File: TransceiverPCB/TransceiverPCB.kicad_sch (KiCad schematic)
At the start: 231 parts, among them IC1 QPL6220QTR7, IC2 AD9218BSTZ-65, IC3 AD9763ASTZ, IC4 ADF4351BCPZ-RL7, J1 USB4085-GF-A_REVB, J2 RFPC-SMA27-F, J3 RFPC-SMA27-F, J4 FPGA JTAG, SW1 SW_Push, SW2 SW_Push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

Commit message: Vocm on ADC and Bias on the ADC driver
- Vocm on ADC driver set to +1V instead of +1v1
- rearranged some ADC pins DFS/GAIN and REFOUT are now closer
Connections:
- no-connect marks 45 -> 46
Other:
- note added: "What is this?"
- note removed: "Can we use the +1V rail instead of +1V1?????"
- note removed: "Can we use the +1V rail instead of +1V1????? Sure"
- moved on the sheet: C1, C121, C122, C123, C129, C130, C131, C132, C2, C3, C30, C31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

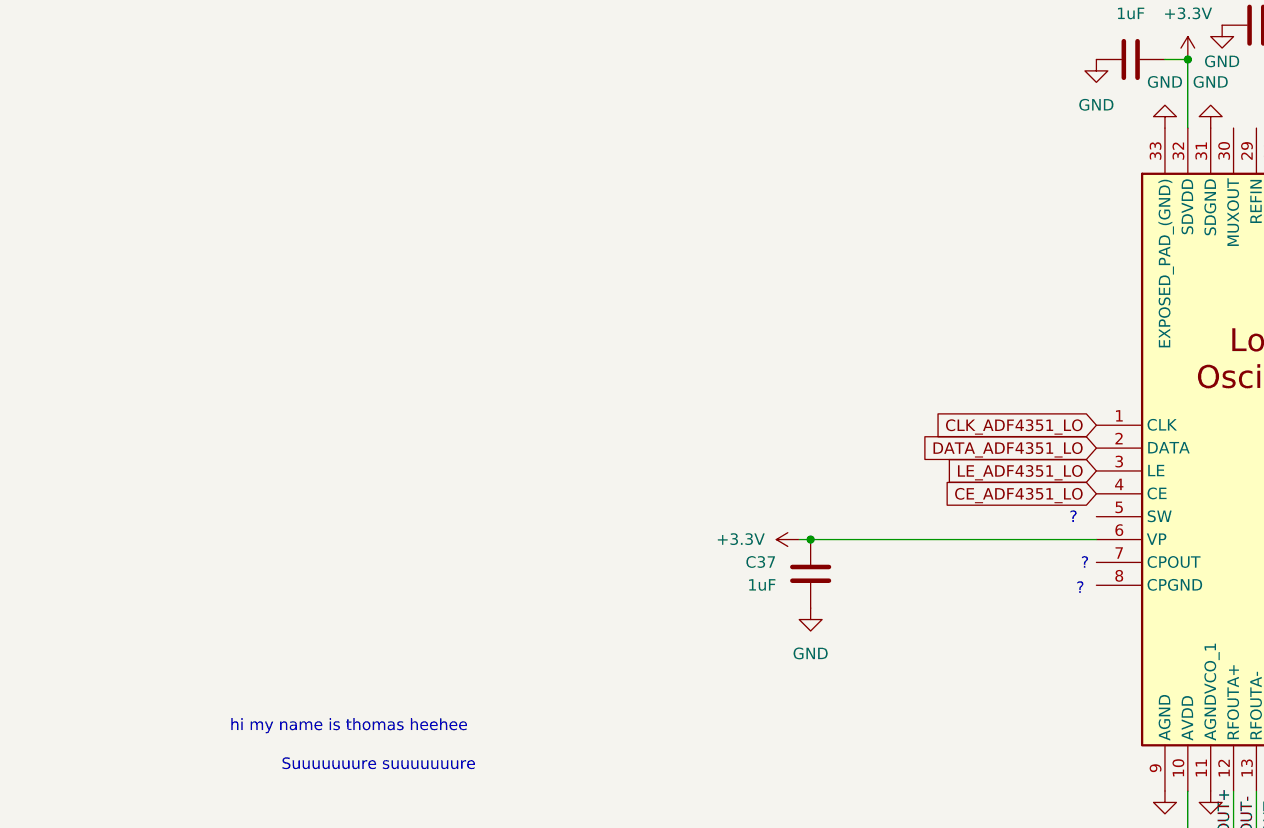
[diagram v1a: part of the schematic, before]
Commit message: Added PLL Filter for LO
-Added PLL filter for LO between pins 7 and 20
-Still need to look into values and how they impact frequency (if at all)
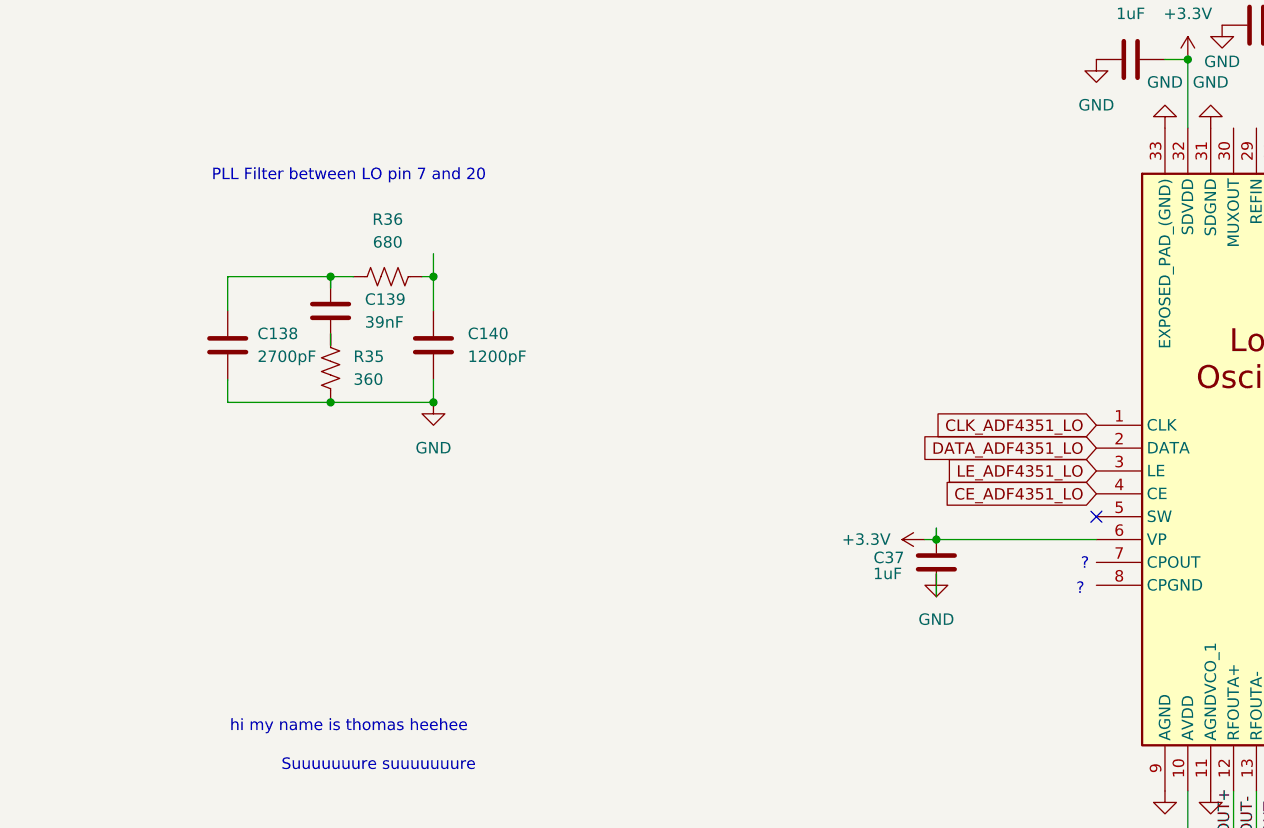
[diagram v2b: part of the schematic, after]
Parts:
- added C138: 2700pF, symbol Device:C
- added C139: 39nF, symbol Device:C
- added C140: 1200pF, symbol Device:C
- added R35: 360, symbol Device:R_US
- added R36: 680, symbol Device:R_US
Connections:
- net GND: now also C138.2, C140.2, R35.2
- new net: C138.1, C139.1, R36.1
- new net: C140.1, R36.2
- new net: C139.2, R35.1
- no-connect marks 46 -> 47
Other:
- note added: "PLL Filter between LO pin 7 and 20"
- moved on the sheet: C37

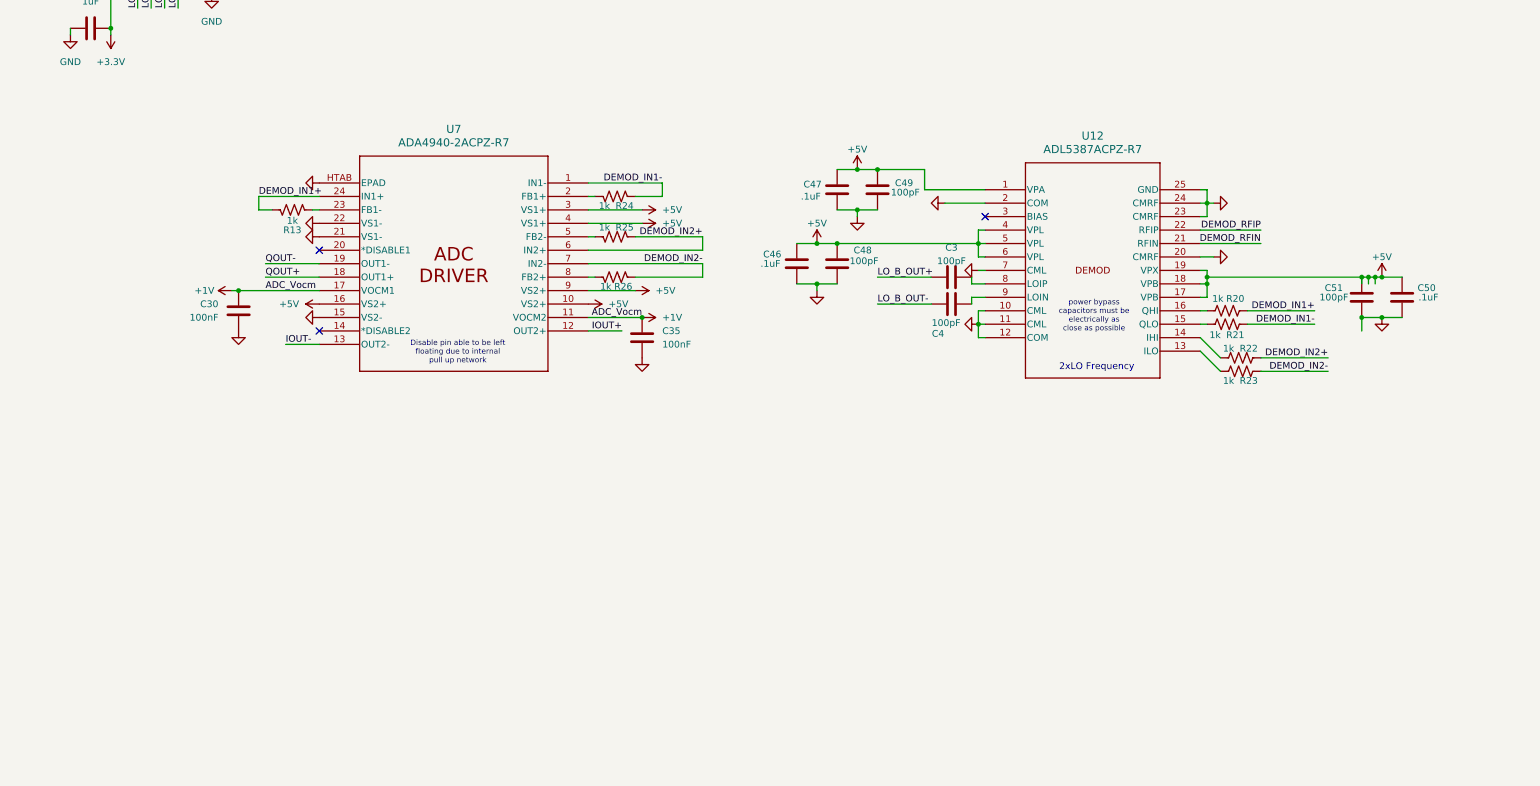
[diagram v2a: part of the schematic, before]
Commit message: Filter from LO to demod
3rd and 5th harmonic filter from LO to demod
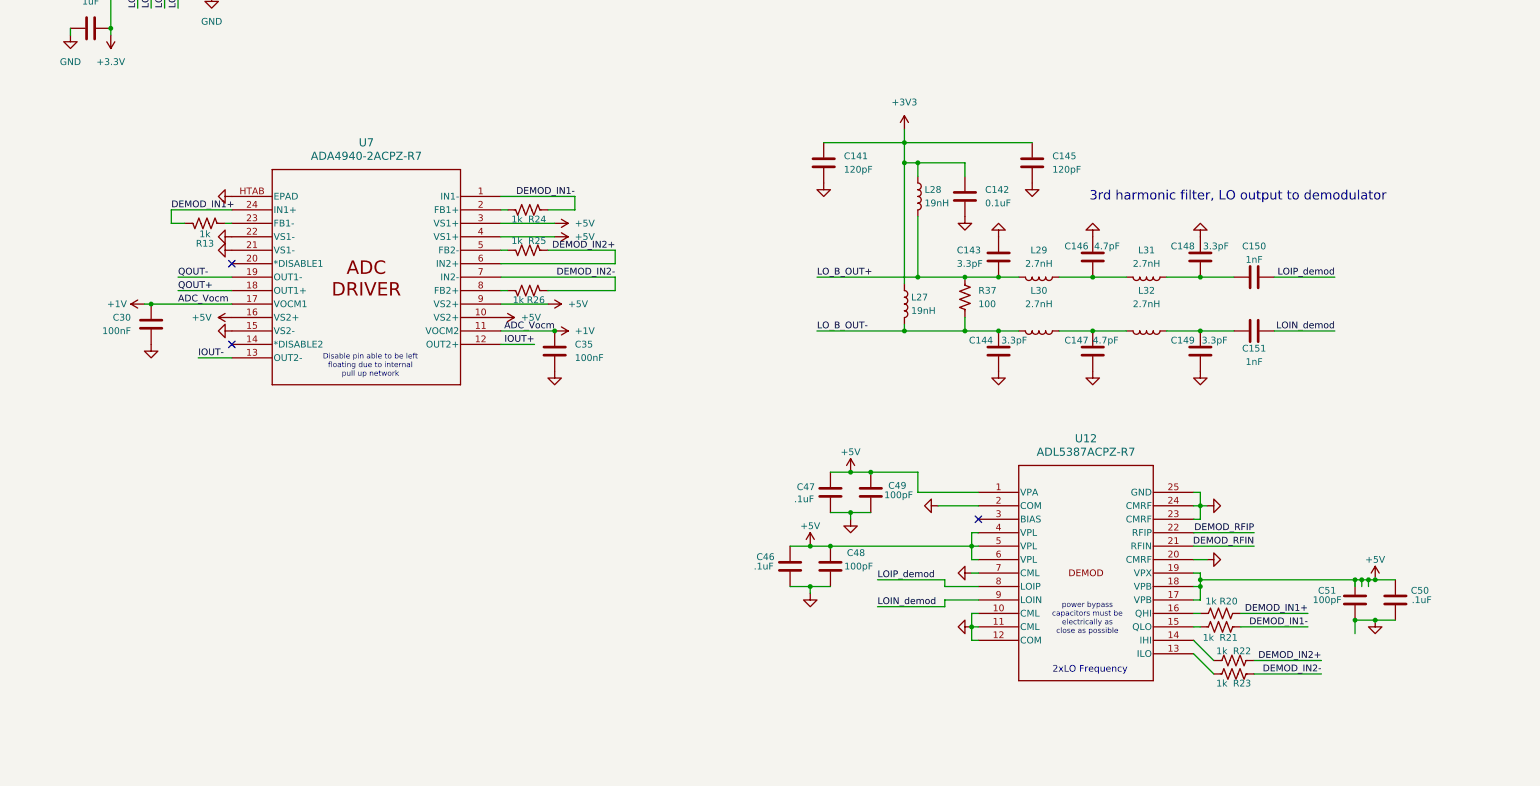
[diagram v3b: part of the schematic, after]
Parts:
- removed C3, C4: 100pF, symbol Device:C
- added C141, C145: 120pF, symbol Device:C
- added C142: 0.1uF, symbol Device:C
- added C143, C144, C148, C149: 3.3pF, symbol Device:C
- added C146, C147: 4.7pF, symbol Device:C
- added C150, C151: 1nF, symbol Device:C
- added L27, L28: 19nH, symbol Device:L
- added L29, L30, L31, L32: 2.7nH, symbol Device:L
- added R37: 100, symbol Device:R_US
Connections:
- net +3V3: now also C141.1, C142.1, C145.1, L27.1, L28.1
- net GND: now also C141.2, C142.2, C143.1, C144.2, C145.2, C146.1, C147.2, C148.1, C149.2
- net LO_B_OUT+: now also C143.2, L28.2, L29.2, R37.1
- net LO_B_OUT-: now also C144.1, L27.2, L30.2, R37.2
- net LOIP_demod: now reaches U12.8 (LOIP)
- net LOIP_demod: now also C150.2
- net LOIN_demod: now reaches U12.9 (LOIN)
- net LOIN_demod: now also C151.2
- new net: C146.2, L29.1, L31.2
- new net: C149.1, C151.1, L32.1
- new net: C148.2, C150.1, L31.1
- new net: C147.1, L30.1, L32.2
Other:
- note added: "3rd harmonic filter, LO output to demodulator"
- moved on the sheet: C30, C35, C46, C47, C48, C49, C50, C51, R13, R20, R21, R22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

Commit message: DAC notes, caps notes
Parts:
- added R38, R39, R40: 10k, symbol Device:R_US
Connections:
- net +3V3: now also U1.E4 (VCCO_35), R38.2, R39.2; no longer U1.E3 (IO_L11P_T1_SRCC_35)
- net FPGA_TCK: now also R40.1
- net FPGA_TDI: now also R38.1
- net FPGA_TMS: now also R39.1
- net GND: now also R40.2
- net SPI0_CS_RP2040_FPGA: now also U1.E3 (IO_L11P_T1_SRCC_35); no longer U1.N13 (IO_L11P_T1_SRCC_14)
- net SPI0_MISO_RP2040_FPGA: now also U1.F5 (IO_L13P_T2_MRCC_35); no longer U1.N11 (IO_L13P_T2_MRCC_14)
- net SPI0_MOSI_RP2040_FPGA: now also U1.E5 (IO_L13N_T2_MRCC_35); no longer U1.N12 (IO_L13N_T2_MRCC_14)
- net SPI0_SCK_RP2040_FPGA: now also U1.D4 (IO_L12P_T1_MRCC_35); no longer U1.N14 (IO_L12P_T1_MRCC_14)
- net CLK1/IQCLK: now reaches U1.C13 (IO_L12N_T1_MRCC_15)
- net CLK1/IQCLK: now also IC3.18 (CLK1/IQCLK), IC3.19 (CLK2/IQRESET)
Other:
- note added: "- Values must be larger than specified - Body size smaller than specified - ESR within specified range - Voltage rating can be higher than specified"
- note added: "Connect pins to bank 14"
- note added: "Connect pins to bank 15"
- note added: "Decoupling Capacitors"

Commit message: DAC stuff
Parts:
- added C152: 0.1uF, symbol Device:C_US
- added C3, C4: 22nF, symbol Device:C
- added R41: 10k, symbol Device:R_US
- added R42, R43: 256, symbol Device:R_US
- added R44: 2k, symbol Device:R_US
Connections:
- net +3V3: now also IC3.42 (GAINCTRL), IC3.43 (REFIO), C152.1, R41.2; no longer IC3.48 (MODE)
- net GND: now also C152.2, C3.2, C4.2, R44.2
- net at IC3.41 (FSADJ2): now also R42.1
- net at IC3.44 (FSADJ1): now also R43.1, R44.1
- new net: IC3.48 (MODE), R41.1
- new net: C4.1, R43.2
- new net: C3.1, R42.2
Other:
- note added: "RSET"
- moved on the sheet: C133
